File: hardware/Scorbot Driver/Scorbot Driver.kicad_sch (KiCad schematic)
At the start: 86 parts, among them Q1 2N7002, Q2 2N7002, Q3 2N7002, Q4 2N7002, Q5 2N7002, U1 24pin ATX PSU Connector, U10 OPB628, U11 OPB628, U2 Raspi Motor Driver HAT, U3 Raspi Motor Driver HAT, U4 MCP23017-E/SP, U5 ADS1015BQDGSRQ1, U6 MCP23017-E/SP, U7 ADS1015BQDGSRQ1, U8 ADS1015BQDGSRQ1, U9 ADS1015BQDGSRQ1

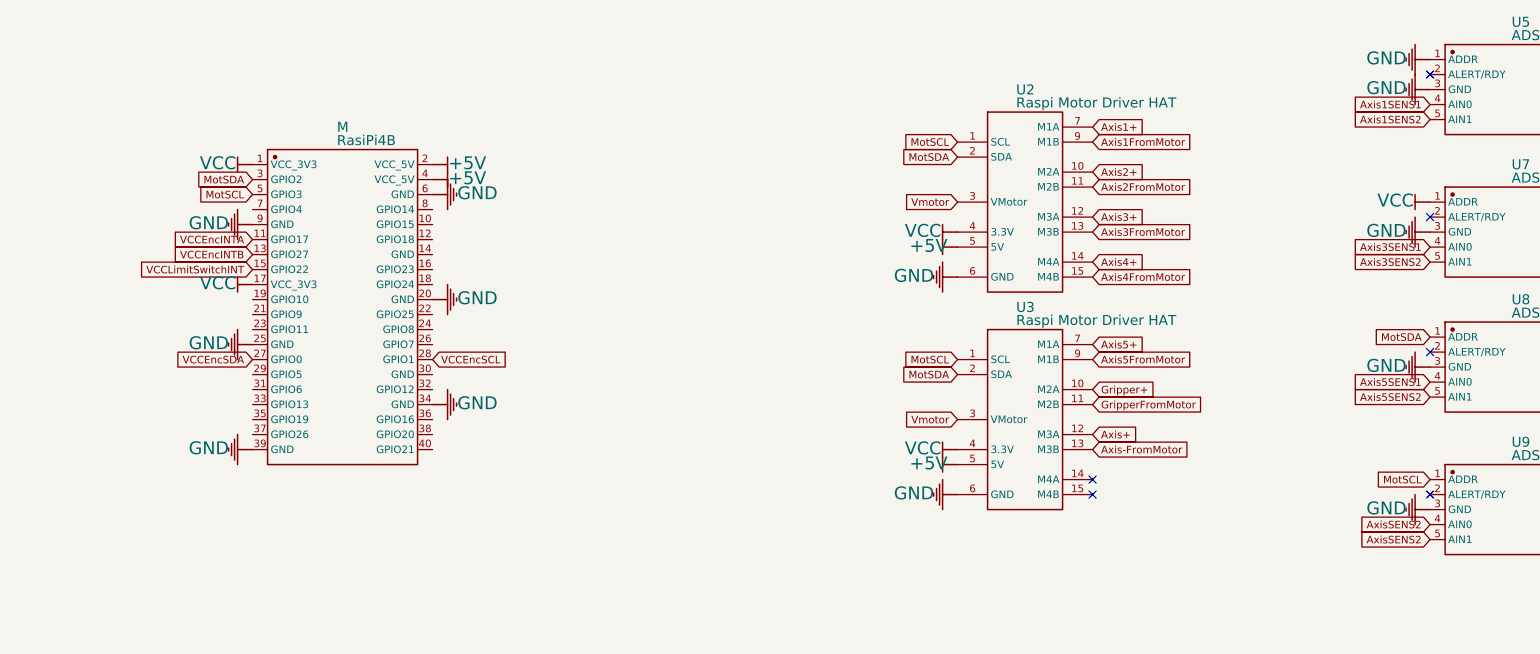
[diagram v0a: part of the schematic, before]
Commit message: hardware schematics ADS1015 Alert pins attached to rPI
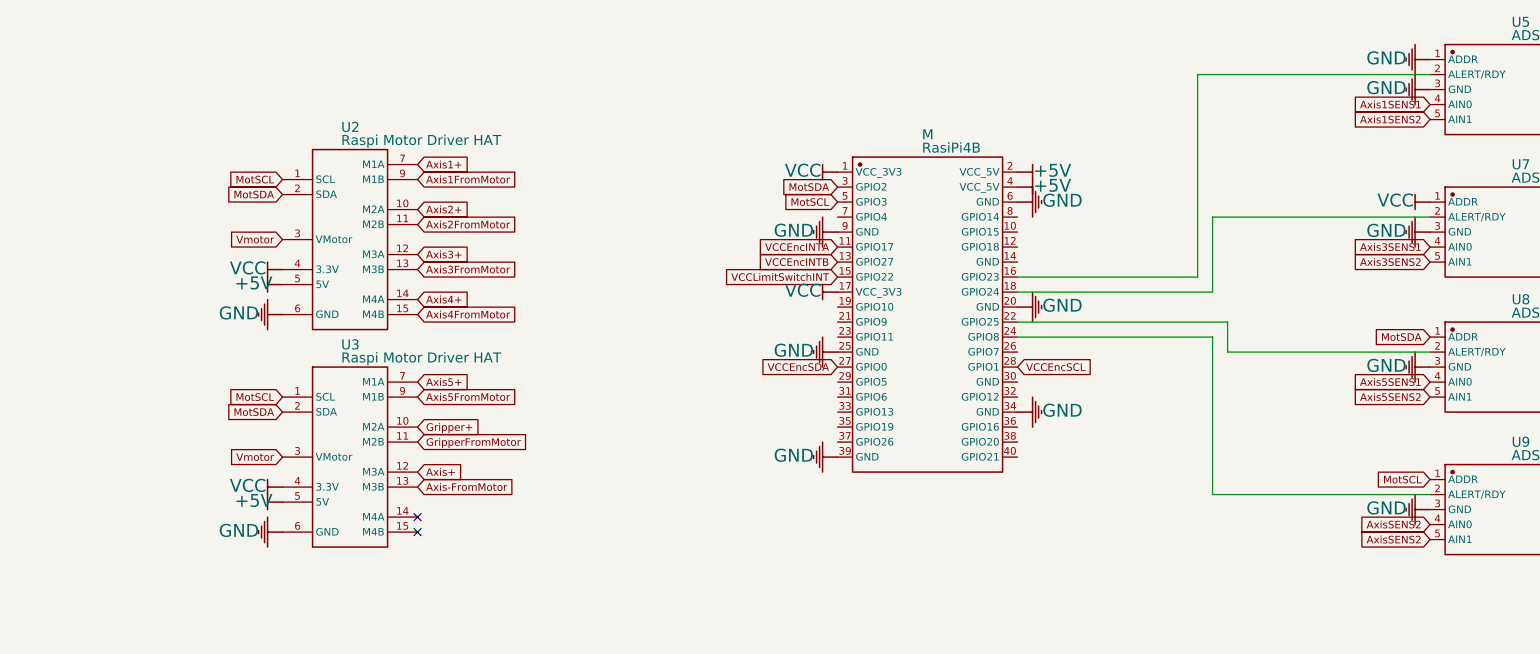
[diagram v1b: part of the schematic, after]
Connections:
- net at M.16 (GPIO23): now also U5.2 (ALERT/RDY)
- net at M.18 (GPIO24): now also U7.2 (ALERT/RDY)
- net at M.22 (GPIO25): now also U8.2 (ALERT/RDY)
- net at M.24 (GPIO8): now also U9.2 (ALERT/RDY)
- no-connect marks 37 -> 33
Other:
- moved on the sheet: M, U2, U3

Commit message: added inductive kickback protection in hardware schematics
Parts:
- removed R1: 0.1, symbol R_0603_US_1
- removed R12: 0.1, symbol R_0603_US_11
- removed R13: 10k, symbol R_0603_US_12
- removed R14: 10k, symbol R_0603_US_13
- removed R15: 5k, symbol R_0603_US_14
- removed R16: 5k, symbol R_0603_US_15
- removed R17: 5k, symbol R_0603_US_16
- removed R18: 5k, symbol R_0603_US_17
- removed R19: 10k, symbol R_0603_US_18
- removed R20: 10k, symbol R_0603_US_19
- removed R21: 0.1, symbol R_0603_US_20
- removed R22: 0.1, symbol R_0603_US_21
- removed R23: 10k, symbol R_0603_US_22
- removed R24: 10k, symbol R_0603_US_23
- removed R25: 5k, symbol R_0603_US_24
- removed R26: 5k, symbol R_0603_US_25
- removed R27: 0.1, symbol R_0603_US_26
- removed R28: 10k, symbol R_0603_US_27
- removed R29: 10k, symbol R_0603_US_28
- removed R3: 10k, symbol R_0603_US_2
- removed R30: 5k, symbol R_0603_US_29
- removed R31: 5k, symbol R_0603_US_30
- removed R32: 5k, symbol R_0603_US_31
- removed R33: 5k, symbol R_0603_US_32
- removed R34: 10k, symbol R_0603_US_33
- removed R35: 10k, symbol R_0603_US_34
- removed R36: 0.1, symbol R_0603_US_35
- removed R4: 10k, symbol R_0603_US_3
- removed R5: 5k, symbol R_0603_US_4
- removed R6: 5k, symbol R_0603_US_5
- removed U3: Raspi Motor Driver HAT, symbol Raspi Motor Driver HAT_1
- added D1, D10, D11, D12, D13, D14, D15, D16, D17, D18, D19, D2, D20, D21, D22, D23, D24, D25, D26, D29, D3, D30, D4, D5, D6, D7, D8, D9: SB550, Diode_THT:D_DO-201AD_P15.24mm_Horizontal, symbol Diode:1N5822
- added R1, R22, R31, R32, R6, R71: 5k, symbol R_0603_US_7
- added R12, R21, R23, R3, R30, R70: 15k, symbol R_0603_US_8
- added R15, R16, R17, R26, R27, R69: 0.1, symbol R_0603_US_10
- added R19, R25, R28, R33, R5, R67: 5k, symbol R_0603_US_6
- added R20, R24, R29, R34, R4, R66: 15k, symbol R_0603_US_9
- added SW: SW_SPDT, symbol Switch:SW_SPDT
- added U12: Raspi Motor Driver HAT, symbol Raspi Motor Driver HAT
- R10, R9: value 10k -> 15k
- renumbered M to M1
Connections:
- net +5V: now also U1.6 (5V), U12.5 (5V); no longer U1.9 (5VSTBY)
- net Axis+: now also D23.2 (A), D24.1 (K), U12.12 (M3A)
- net Axis-: now also D19.2 (A), D20.1 (K), R17.1, R34.2
- net Axis1+: now also D7.2 (A), D8.1 (K)
- net Axis1-: now also D5.2 (A), D6.1 (K), R66.2, R69.1; no longer R10.2, R11.1
- net Axis1SENS1: now also R70.1, R71.2; no longer R10.1, R7.2
- net Axis1SENS2: no longer R8.2, R9.1
- net Axis2+: now also D1.2 (A), D4.1 (K)
- net Axis2-: now also R11.2, R9.2, D2.2 (A), D3.1 (K)
- net Axis2SENS1: now also R10.1, R7.2
- net Axis2SENS2: now also R8.2, R9.1
- net Axis3+: now also D11.2 (A), D12.1 (K)
- net Axis3-: now also D10.1 (K), D9.2 (A), R26.1, R29.2
- net Axis3SENS1: now also R22.2, R23.1
- net Axis4+: now also D13.2 (A), D14.1 (K)
- net Axis4-: now also D15.2 (A), D16.1 (K), R27.2, R30.2
- net Axis4SENS1: now also R24.1, R25.2
- net Axis4SENS2: now also R30.1, R31.2
- net Axis5+: now also D21.2 (A), D22.1 (K), U12.7 (M1A)
- net Axis5-: now also D17.2 (A), D18.1 (K), R15.1, R20.2
- net Axis5SENS1: now also R1.2, R3.1
- net AxisSENS1: now also R12.1, R6.2
- net GND: now also D10.2 (A), D12.2 (A), D14.2 (A), D16.2 (A), D18.2 (A), D20.2 (A), D22.2 (A), D24.2 (A), D26.2 (A), D3.2 (A), D30.2 (A), D4.2 (A), D6.2 (A), D8.2 (A), R1.1, R19.1, R22.1, R25.1, R28.1, R31.1, R32.1, R33.1, R5.1, R6.1, R67.1, R71.1, U12.6 (GND)
- net Gripper+: now also D25.2 (A), D26.1 (K), U12.10 (M2A)
- net Gripper-: now also D29.2 (A), D30.1 (K), R16.2, R21.2
- net GripperSENS1: now also R4.1, R5.2
- net GripperSENS2: now also R21.1, R32.2
- net MotSCL: now also U12.1 (SCL)
- net MotSDA: now also U12.2 (SDA)
- net VCC: now also U12.4 (3.3V)
- net at U1.19 (GND): now also SW.3 (C)
- removed net Axis1FromMotor: R11.2, R9.2, U2.9 (M1B)
- net Axis2FromMotor: no longer names the net of U2.11 (M2B)
- net Axis2FromMotor: now also R10.2, R11.1
- net Axis3FromMotor: no longer names the net of U2.13 (M3B)
- net Axis3FromMotor: now also R23.2, R26.2
- net Axis4FromMotor: no longer names the net of U2.15 (M4B)
- net Axis4FromMotor: now also R24.2, R27.1
- net PS_On: no longer names the net of U1.16 (PS_ON)
- net PS_On: now also SW.2 (B)
- net PW_Good: no longer names the net of U1.8 (PW_G)
- net Vmotor renamed +12V
- net +12V: now also D1.1 (K), D11.1 (K), D13.1 (K), D15.1 (K), D17.1 (K), D19.1 (K), D2.1 (K), D21.1 (K), D23.1 (K), D25.1 (K), D29.1 (K), D5.1 (K), D7.1 (K), D9.1 (K), U12.3 (VMotor)
- new net: R12.2, R17.2, U12.13 (M3B)
- new net: R69.2, R70.2, U2.9 (M1B)
- new net: R19.2, R20.1
- new net: R33.2, R34.1
- new net: R66.1, R67.2
- new net: R28.2, R29.1
- new net: R15.2, R3.2, U12.9 (M1B)
- new net: R16.1, R4.2, U12.11 (M2B)
- no-connect marks 33 -> 48
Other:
- note added: "+ to A, - to B"
- note added: "Emergency-stop"
- note added: "Inductive Kickback Protection"
- note added: "Voltage Divider to convert 12v to ~3 volt"
- note removed: "Voltage Divider to convert 12v to ~5 volt"
- moved on the sheet: M1, R10, R11, R7, R8, R9, U2, U5, U7, U8, U9
